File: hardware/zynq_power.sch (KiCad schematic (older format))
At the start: 61 parts, among them U1 xc7z030sbg485

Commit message: Added Power/Protection Circuit
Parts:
- renumbered C1 to C201, C2 to C202, C3 to C203, C4 to C204, C5 to C205, C6 to C206, C7 to C207, C8 to C208, C9 to C209, C10 to C210, C11 to C211, C12 to C212, C13 to C213, C14 to C214, C15 to C215, C16 to C216, C17 to C217, C18 to C218, C19 to C219, C20 to C220, C21 to C221, C22 to C222, C23 to C223, C24 to C224, C25 to C225, C26 to C226, C27 to C227, C28 to C228, C29 to C229, C30 to C230, C31 to C231, C32 to C232, C33 to C233, C34 to C234, C35 to C235, C36 to C236, C37 to C237, C38 to C238, C39 to C239, C40 to C240, C41 to C241, C42 to C242, C43 to C243, C44 to C244, C45 to C245, C46 to C246, C47 to C247, C48 to C248, C49 to C249, C50 to C250, C51 to C251, C52 to C252, C53 to C253, C54 to C254, C55 to C255, C56 to C256, C57 to C257, C58 to C258, L1 to L201, L2 to L202, U1 to U201

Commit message: Length matched DDR3 Memory again.
Forgot to keep enough space between the traces and between the meander waves.

Also, I switched to Kicad 5.0 RC2.

Swaped a few ddr signals.
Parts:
- C201, C203, C204, C205, C206, C208, C209, C210, C211, C212, C213, C214, C215, C216, C217, C218, C219, C220, C223, C224, C225, C226, C227, C228, C229, C230, C231, C233, C234, C235, C236, C237, C238, C239, C240, C241, C242, C243, C244, C245, C246, C247, C249, C250, C251, C252, C253, C255, C256, C257, C258: symbol C_Small -> device:C_Small
- C202: footprint C_2917 -> (none); symbol CP_Small -> device:CP_Small
- C207, C221, C222, C232, C248, C254: symbol CP_Small -> device:CP_Small
- L201, L202: symbol L_Small -> device:L_Small
- U201: symbol xc7z030sbg485 -> xilinx_zynq_clg485:xc7z030sbg485
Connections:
- wire segments 184 -> 292

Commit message: Layouted most of the Power Circuit and Triggerbus Levelshifters.
Added Footprint for Tantal Caps. Modified Footprint for MDR20 Connector, SD-Card.

Fixed Symbol and Circuit for Power Supervisor/Delay IC.

Also fixed some smaller things in the schematics.
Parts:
- C201, C203, C234, C239: footprint Capacitors_SMD:C_1210 -> Capacitor_SMD:C_0603_1608Metric; Description CAP CER 47UF 6.3V X5R 1210 -> CAP CER 47UF 6.3V X5R 0603; Digikey 490-1887-1-ND -> 490-13247-1-ND; MFG Part Num GRM32ER60J476ME20L -> GRM188R60J476ME15D; Populate for CLG484(Z-7012s/Z-7015) (none) -> 1; Populate for SBGA485(Z-7030) (none) -> 1; Voltage (none) -> 6,3 V
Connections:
- net labels added: MGTAVCC, MGTAVTT
- wire segments 292 -> 294
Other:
- note added: "Todo: for MGTAVCC and MGTAVTT each add two 100 nF 0201 Cap and 1x 4.7 µF"
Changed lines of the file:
@@
 F 0 "C234" H 5260 1570 50  0000 L CNN
 F 1 "47µF" H 5260 1420 50  0000 L CNN
-F 2 "Capacitors_SMD:C_1210" H 5250 1500 50  0001 C CNN
-F 3 "http://search.murata.co.jp/Ceramy/image/img/A01X/G101/ENG/GRM32ER60J476ME20-01.pdf" H 5250 1500 50  0001 C CNN
+F 2 "Capacitor_SMD:C_0603_1608Metric" H 5250 1500 50  0001 C CNN
+F 3 "http://search.murata.co.jp/Ceramy/image/img/A01X/G101/ENG/GRM188R60J476ME15-01.pdf" H 5250 1500 50  0001 C CNN
 F 4 "Murata" H 5250 1500 60  0001 C CNN "MFG Name"
-F 5 "GRM32ER60J476ME20L" H 5250 1500 60  0001 C CNN "MFG Part Num"
-F 6 "490-1887-1-ND" H 5250 1500 60  0001 C CNN "Digikey"
+F 5 "GRM188R60J476ME15D " H 5250 1500 60  0001 C CNN "MFG Part Num"
+F 6 "490-13247-1-ND" H 5250 1500 60  0001 C CNN "Digikey"
 F 7 "1" H 5250 1500 60  0001 C CNN "Populated"
-F 8 "CAP CER 47UF 6.3V X5R 1210" H 5250 1500 60  0001 C CNN "Description"
+F 8 "CAP CER 47UF 6.3V X5R 0603" H 5250 1500 60  0001 C CNN "Description"
 F 9 "SPEC" H 5250 1500 60  0001 C CNN "Source"
+F 10 "1" H 5250 1500 50  0001 C CNN "Populate for SBGA485(Z-7030)"
+F 11 "1" H 5250 1500 50  0001 C CNN "Populate for CLG484(Z-7012s/Z-7015)"
+F 12 "6,3 V" H 5350 1300 50  0000 C BNN "Voltage"
 	1    5250 1500
 	1    0    0    -1
@@
 $EndComp
 $Comp
-L device:C_Small C203
-U 1 1 5AE7068A
-P 1200 3550
-F 0 "C203" H 1210 3620 50  0000 L CNN
-F 1 "47µF" H 1210 3470 50  0000 L CNN
-F 2 "Capacitors_SMD:C_1210" H 1200 3550 50  0001 C CNN
-F 3 "http://search.murata.co.jp/Ceramy/image/img/A01X/G101/ENG/GRM32ER60J476ME20-01.pdf" H 1200 3550 50  0001 C CNN
-F 4 "Murata" H 1200 3550 60  0001 C CNN "MFG Name"
-F 5 "GRM32ER60J476ME20L" H 1200 3550 60  0001 C CNN "MFG Part Num"
-F 6 "490-1887-1-ND" H 1200 3550 60  0001 C CNN "Digikey"
-F 7 "1" H 1200 3550 60  0001 C CNN "Populated"
-F 8 "CAP CER 47UF 6.3V X5R 1210" H 1200 3550 60  0001 C CNN "Description"
-F 9 "SPEC" H 1200 3550 60  0001 C CNN "Source"
-	1    1200 3550
-	1    0    0    -1
-$EndComp
-$Comp
 L device:CP_Small C207
 U 1 1 5AE72084
@@
 VCCO_MIO1
 $Comp
-L device:C_Small C201
-U 1 1 5AE73C22
-P 800 5450
-F 0 "C201" H 810 5520 50  0000 L CNN
-F 1 "47µF" H 810 5370 50  0000 L CNN
-F 2 "Capacitors_SMD:C_1210" H 800 5450 50  0001 C CNN
-F 3 "http://search.murata.co.jp/Ceramy/image/img/A01X/G101/ENG/GRM32ER60J476ME20-01.pdf" H 800 5450 50  0001 C CNN
-F 4 "Murata" H 800 5450 60  0001 C CNN "MFG Name"
-F 5 "GRM32ER60J476ME20L" H 800 5450 60  0001 C CNN "MFG Part Num"
-F 6 "490-1887-1-ND" H 800 5450 60  0001 C CNN "Digikey"
-F 7 "1" H 800 5450 60  0001 C CNN "Populated"
-F 8 "CAP CER 47UF 6.3V X5R 1210" H 800 5450 60  0001 C CNN "Description"
-F 9 "SPEC" H 800 5450 60  0001 C CNN "Source"
-	1    800  5450
-	1    0    0    -1
-$EndComp
-$Comp
 L power1:GND #PWR06
 U 1 1 5AE7C463
@@
 Text GLabel 4450 5100 1    60   Output ~ 0
 VCCO_34
-$Comp
-L device:C_Small C239
-U 1 1 5AE90BAB
-P 5950 5450
-F 0 "C239" H 5960 5520 50  0000 L CNN
-F 1 "47µF" H 5960 5370 50  0000 L CNN
-F 2 "Capacitors_SMD:C_1210" H 5950 5450 50  0001 C CNN
-F 3 "http://search.murata.co.jp/Ceramy/image/img/A01X/G101/ENG/GRM32ER60J476ME20-01.pdf" H 5950 5450 50  0001 C CNN
-F 4 "Murata" H 5950 5450 60  0001 C CNN "MFG Name"
-F 5 "GRM32ER60J476ME20L" H 5950 5450 60  0001 C CNN "MFG Part Num"
-F 6 "490-1887-1-ND" H 5950 5450 60  0001 C CNN "Digikey"
-F 7 "1" H 5950 5450 60  0001 C CNN "Populated"
-F 8 "CAP CER 47UF 6.3V X5R 1210" H 5950 5450 60  0001 C CNN "Description"
-F 9 "SPEC" H 5950 5450 60  0001 C CNN "Source"
-	1    5950 5450
-	1    0    0    -1
-$EndComp
 $Comp
 L power1:GND #PWR017
@@
 Wire Wire Line
 	1200 3300 1200 3200
+$Comp
+L device:C_Small C203
+U 1 1 5B120C73
+P 1200 3550
+F 0 "C203" H 1210 3620 50  0000 L CNN
+F 1 "47µF" H 1210 3470 50  0000 L CNN
+F 2 "Capacitor_SMD:C_0603_1608Metric" H 1200 3550 50  0001 C CNN
+F 3 "http://search.murata.co.jp/Ceramy/image/img/A01X/G101/ENG/GRM188R60J476ME15-01.pdf" H 1200 3550 50  0001 C CNN
+F 4 "Murata" H 1200 3550 60  0001 C CNN "MFG Name"
+F 5 "GRM188R60J476ME15D " H 1200 3550 60  0001 C CNN "MFG Part Num"
+F 6 "490-13247-1-ND" H 1200 3550 60  0001 C CNN "Digikey"
+F 7 "1" H 1200 3550 60  0001 C CNN "Populated"
+F 8 "CAP CER 47UF 6.3V X5R 0603" H 1200 3550 60  0001 C CNN "Description"
+F 9 "SPEC" H 1200 3550 60  0001 C CNN "Source"
+F 10 "1" H 1200 3550 50  0001 C CNN "Populate for SBGA485(Z-7030)"
+F 11 "1" H 1200 3550 50  0001 C CNN "Populate for CLG484(Z-7012s/Z-7015)"
+F 12 "6,3 V" H 1300 3350 50  0000 C BNN "Voltage"
+	1    1200 3550
+	1    0    0    -1
+$EndComp
+$Comp
+L device:C_Small C239
+U 1 1 5B120EBB
+P 5950 5450
+F 0 "C239" H 5960 5520 50  0000 L CNN
+F 1 "47µF" H 5960 5370 50  0000 L CNN
+F 2 "Capacitor_SMD:C_0603_1608Metric" H 5950 5450 50  0001 C CNN
+F 3 "http://search.murata.co.jp/Ceramy/image/img/A01X/G101/ENG/GRM188R60J476ME15-01.pdf" H 5950 5450 50  0001 C CNN
+F 4 "Murata" H 5950 5450 60  0001 C CNN "MFG Name"
+F 5 "GRM188R60J476ME15D " H 5950 5450 60  0001 C CNN "MFG Part Num"
+F 6 "490-13247-1-ND" H 5950 5450 60  0001 C CNN "Digikey"
+F 7 "1" H 5950 5450 60  0001 C CNN "Populated"
+F 8 "CAP CER 47UF 6.3V X5R 0603" H 5950 5450 60  0001 C CNN "Description"
+F 9 "SPEC" H 5950 5450 60  0001 C CNN "Source"
+F 10 "1" H 5950 5450 50  0001 C CNN "Populate for SBGA485(Z-7030)"
+F 11 "1" H 5950 5450 50  0001 C CNN "Populate for CLG484(Z-7012s/Z-7015)"
+F 12 "6,3 V" H 6050 5250 50  0000 C BNN "Voltage"
+	1    5950 5450
+	1    0    0    -1
+$EndComp
+$Comp
+L device:C_Small C201
+U 1 1 5B121187
+P 800 5450
+F 0 "C201" H 810 5520 50  0000 L CNN
+F 1 "47µF" H 810 5370 50  0000 L CNN
+F 2 "Capacitor_SMD:C_0603_1608Metric" H 800 5450 50  0001 C CNN
+F 3 "http://search.murata.co.jp/Ceramy/image/img/A01X/G101/ENG/GRM188R60J476ME15-01.pdf" H 800 5450 50  0001 C CNN
+F 4 "Murata" H 800 5450 60  0001 C CNN "MFG Name"
+F 5 "GRM188R60J476ME15D " H 800 5450 60  0001 C CNN "MFG Part Num"
+F 6 "490-13247-1-ND" H 800 5450 60  0001 C CNN "Digikey"
+F 7 "1" H 800 5450 60  0001 C CNN "Populated"
+F 8 "CAP CER 47UF 6.3V X5R 0603" H 800 5450 60  0001 C CNN "Description"
+F 9 "SPEC" H 800 5450 60  0001 C CNN "Source"
+F 10 "1" H 800 5450 50  0001 C CNN "Populate for SBGA485(Z-7030)"
+F 11 "1" H 800 5450 50  0001 C CNN "Populate for CLG484(Z-7012s/Z-7015)"
+F 12 "6,3 V" H 900 5250 50  0000 C BNN "Voltage"
+	1    800  5450
+	1    0    0    -1
+$EndComp
+Wire Wire Line
+	9800 1350 7200 1350
+Connection ~ 9800 1350
+Wire Wire Line
+	9250 1450 7200 1450
+Connection ~ 9250 1450
+Text Label 7200 1350 0    50   ~ 0
+MGTAVCC
+Text Label 7200 1450 0    50   ~ 0
+MGTAVTT
+Text Label 1600 6550 0    50   ~ 0
+MGTAVCC
+Text Label 2750 6500 0    50   ~ 0
+MGTAVTT
+Text Notes 1200 6800 0    50   ~ 0
+Todo: for MGTAVCC and MGTAVTT each add two 100 nF 0201 Cap and 1x 4.7 µF
 $EndSCHEMATC

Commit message: Improved Powerdistribution Network of the FPGA.
Also started to layout USB.
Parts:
- added C259, C262: 4.7µF, Capacitor_SMD:C_0603_1608Metric, symbol device:C_Small
- added C260, C261, C263, C264: 100 nF, Capacitor_SMD:C_0201_0603Metric, symbol device:C_Small
- C204, C206, C236, C237: footprint Capacitors_SMD:C_0805 -> Capacitor_SMD:C_0603_1608Metric; Description CAP CER 4.7UF 10V X7R 0805 -> CAP CER 4.7UF 6.3V X7R 0603; Digikey 490-6479-1-ND -> 587-4906-1-ND; MFG Name Murata -> Taiyo Yuden; MFG Part Num GRM21BR71A475KA73 -> JMK107BB7475MA-T; Populate for CLG484(Z-7012s/Z-7015) Populate -> 1; Populate for SBGA485(Z-7030) DNP -> 1; Voltage (none) -> 6,3 V
- C205, C224, C251, C256: footprint Capacitors_SMD:C_0805 -> Capacitor_SMD:C_0603_1608Metric; Description CAP CER 4.7UF 10V X7R 0805 -> CAP CER 4.7UF 6.3V X7R 0603; Digikey 490-6479-1-ND -> 587-4906-1-ND; MFG Name Murata -> Taiyo Yuden; MFG Part Num GRM21BR71A475KA73 -> JMK107BB7475MA-T; Populate for CLG484(Z-7012s/Z-7015) (none) -> Populate; Populate for SBGA485(Z-7030) (none) -> DNP; Voltage (none) -> 6,3 V
- C207, C221, C222, C232, C248, C254: footprint Capacitors_SMD:C_1210 -> Capacitor_SMD:C_1210_3225Metric
- C208, C211, C223, C225, C243, C245: footprint Capacitors_SMD:C_0805 -> Capacitor_SMD:C_0603_1608Metric; Description CAP CER 4.7UF 10V X7R 0805 -> CAP CER 4.7UF 6.3V X7R 0603; Digikey 490-6479-1-ND -> 587-4906-1-ND; MFG Name Murata -> Taiyo Yuden; MFG Part Num GRM21BR71A475KA73 -> JMK107BB7475MA-T; Voltage (none) -> 6,3 V
- C209, C210, C212, C213, C214, C215, C216, C217, C218, C219, C220, C228, C230, C231, C233, C235, C238, C240, C241, C242, C244, C246, C247, C249, C250, C252: footprint Capacitors_SMD:C_0603 -> Capacitor_SMD:C_0402_1005Metric; Description CAP CER 0.47UF 6.3V X7R 0603,1 mΩ < ESR < 20 mΩ, ESL 0.5 nH -> CAP CER 0.47UF 6.3V X7R 0402; Digikey 490-6416-1-ND -> 587-3765-1-ND; MFG Name Murata -> Taiyo Yuden; MFG Part Num GRM188R70J474KA01 -> JMK105B7474KVHF; Voltage (none) -> 6.3 V
- C226: footprint Capacitors_SMD:C_0805 -> Capacitor_SMD:C_0603_1608Metric; Description CAP CER 4.7UF 10V X7R 0805 -> CAP CER 4.7UF 6.3V X7R 0603; Digikey 490-6479-1-ND -> 587-4906-1-ND; MFG Name Murata -> Taiyo Yuden; MFG Part Num GRM21BR71A475KA73 -> JMK107BB7475MA-T; Populate for CLG484(Z-7012s/Z-7015) (none) -> 1; Populate for SBGA485(Z-7030) (none) -> 1; Voltage (none) -> 6,3 V
- C227, C229, C253, C257: footprint Capacitors_SMD:C_0603 -> Capacitor_SMD:C_0402_1005Metric; Description CAP CER 0.47UF 6.3V X7R 0603,1 mΩ < ESR < 20 mΩ, ESL 0.5 nH -> CAP CER 0.47UF 6.3V X7R 0402; Digikey 490-6416-1-ND -> 587-3765-1-ND; MFG Name Murata -> Taiyo Yuden; MFG Part Num GRM188R70J474KA01 -> JMK105B7474KVHF; Populate for CLG484(Z-7012s/Z-7015) (none) -> 1; Populate for SBGA485(Z-7030) (none) -> 1; Voltage (none) -> 6.3 V
- C255: footprint Capacitors_SMD:C_0603 -> Capacitor_SMD:C_0603_1608Metric
- C258: footprint Capacitors_SMD:C_0603 -> Capacitor_SMD:C_0402_1005Metric; Description CAP CER 0.47UF 6.3V X5R 0603 -> CAP CER 0.47UF 6.3V X7R 0402; Digikey 490-3266-1-ND -> 587-3765-1-ND; MFG Name Murata -> Taiyo Yuden; MFG Part Num GRM155R60J474KE19D -> JMK105B7474KVHF; Populate for CLG484(Z-7012s/Z-7015) (none) -> 1; Populate for SBGA485(Z-7030) (none) -> 1; Voltage (none) -> 6.3 V
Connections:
- wire segments 294 -> 318

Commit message: Fixed Schematic Symbols
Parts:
- C201, C203, C204, C205, C206, C208, C209, C210, C211, C212, C213, C214, C215, C216, C217, C218, C219, C220, C223, C224, C225, C226, C227, C228, C229, C230, C231, C233, C234, C235, C236, C237, C238, C239, C240, C241, C242, C243, C244, C245, C246, C247, C249, C250, C251, C252, C253, C255, C256, C257, C258, C259, C260, C261, C262, C263, C264: symbol device:C_Small -> Device:C_Small
- C202, C207, C221, C222, C232, C248, C254: symbol device:CP_Small -> Device:CP_Small
- L201, L202: symbol device:L_Small -> Device:L_Small

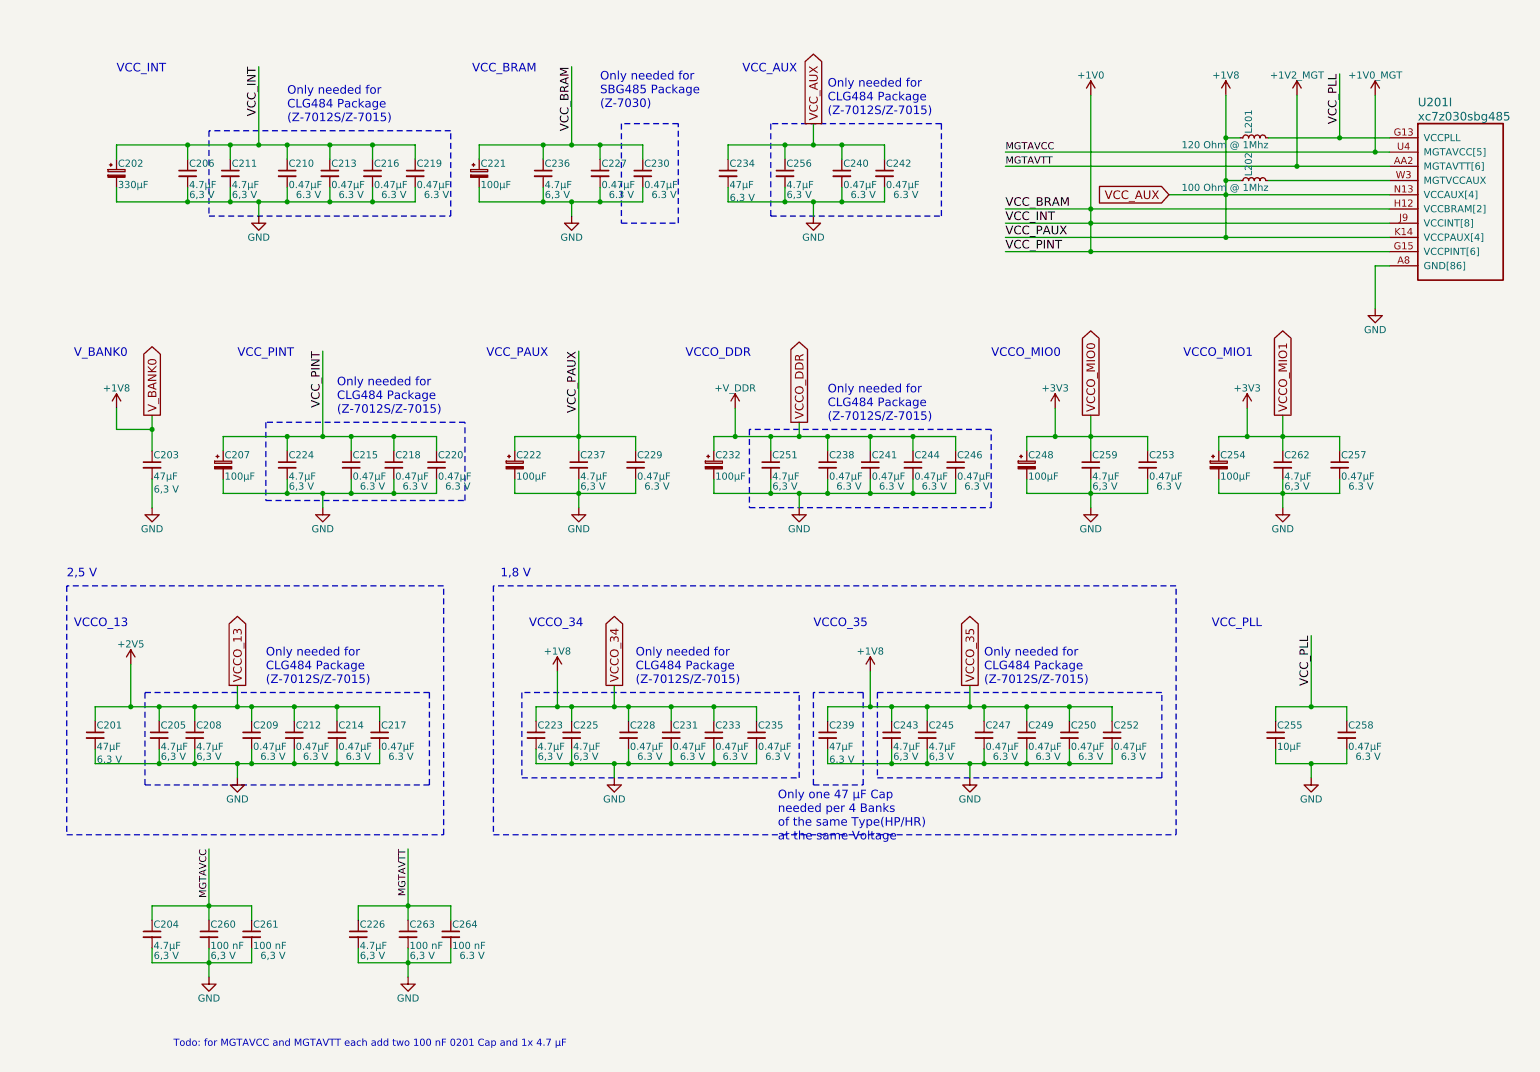
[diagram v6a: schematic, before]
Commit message: SFP+ Power Filter, Levelshifter and MGT/TLK Clock Distribution.
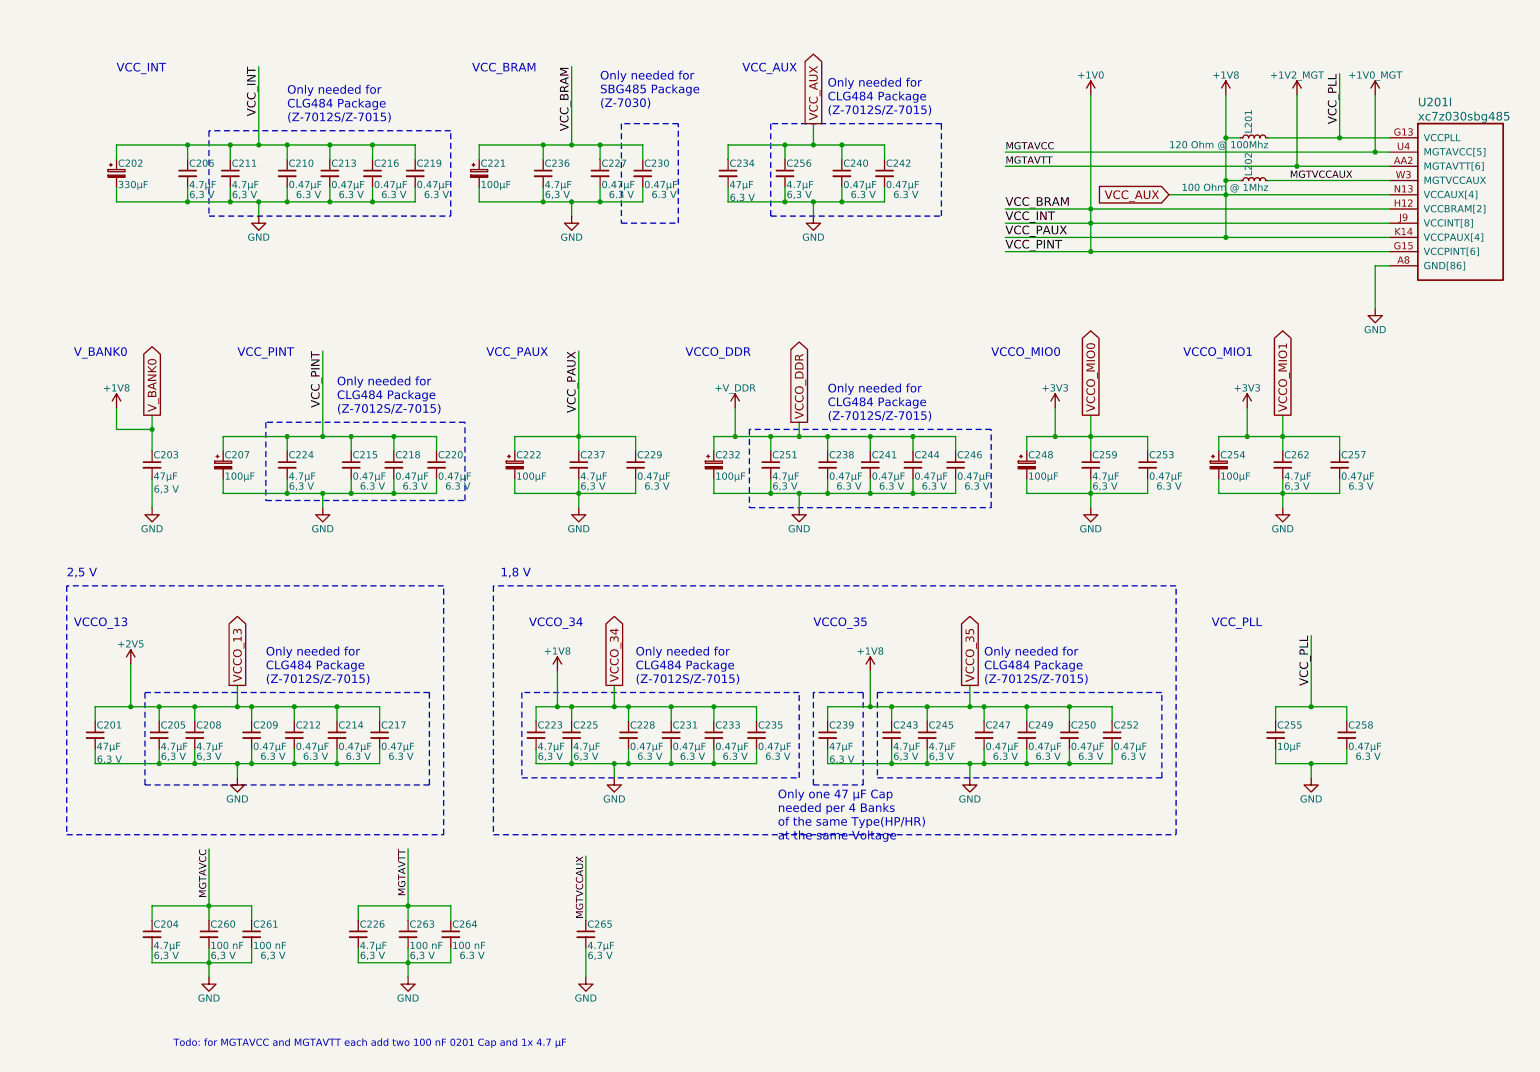
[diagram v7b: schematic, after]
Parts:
- added C265: 4.7µF, Capacitor_SMD:C_0603_1608Metric, symbol Device:C_Small
- L201: value 120 Ohm @ 1Mhz -> 120 Ohm @ 100Mhz
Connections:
- net GND: now also C265.2
- net MGTVCCAUX: now reaches L202.2, U201.W3 (MGTVCCAUX)
- net MGTVCCAUX: now also C265.1
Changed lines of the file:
@@
 P 8950 1250
 F 0 "L201" H 8980 1290 50  0000 L CNN
-F 1 "120 Ohm @ 1Mhz" V 8900 1150 50  0000 L CNN
+F 1 "120 Ohm @ 100Mhz" V 8900 1150 50  0000 L CNN
 F 2 "Inductors_SMD:L_0603" H 8950 1250 50  0001 C CNN
 F 3 "https://www.murata.com/en-us/products/productdata/8796738650142/ENFA0003.pdf" H 8950 1250 50  0001 C CNN
@@
 Wire Wire Line
 	1750 1300 1750 1400
+Text Label 9200 1550 0    50   ~ 0
+MGTVCCAUX
+Text Label 4250 6300 3    50   ~ 0
+MGTVCCAUX
+$Comp
+L Device:C_Small C265
+U 1 1 5BB74A7C
+P 4250 6850
+F 0 "C265" H 4260 6920 50  0000 L CNN
+F 1 "4.7µF" H 4260 6770 50  0000 L CNN
+F 2 "Capacitor_SMD:C_0603_1608Metric" H 4250 6850 50  0001 C CNN
+F 3 "http://ds.yuden.co.jp/TYCOMPAS/ut/detail.do?productNo=JMK107BB7475MA-T&fileName=JMK107BB7475MA-T_SS&mode=specSheetDownload" H 4250 6850 50  0001 C CNN
+F 4 "Taiyo Yuden" H 4250 6850 60  0001 C CNN "MFG Name"
+F 5 "JMK107BB7475MA-T" H 4250 6850 60  0001 C CNN "MFG Part Num"
+F 6 "587-4906-1-ND" H 4250 6850 60  0001 C CNN "Digikey"
+F 7 "1" H 4250 6850 60  0001 C CNN "Populated"
+F 8 "CAP CER 4.7UF 6.3V X7R 0603" H 4250 6850 60  0001 C CNN "Description"
+F 9 "SPEC" H 4250 6850 60  0001 C CNN "Source"
+F 10 "1" H 4250 6850 60  0001 C CNN "Populate for SBGA485(Z-7030)"
+F 11 "1" H 4250 6850 60  0001 C CNN "Populate for CLG484(Z-7012s/Z-7015)"
+F 12 "6,3 V" H 4350 6700 50  0000 C CNN "Voltage"
+	1    4250 6850
+	1    0    0    -1
+$EndComp
+$Comp
+L power:GND #PWR0241
+U 1 1 5BB74B59
+P 4250 7150
+F 0 "#PWR0241" H 4250 6900 50  0001 C CNN
+F 1 "GND" H 4250 7000 50  0000 C CNN
+F 2 "" H 4250 7150 50  0001 C CNN
+F 3 "" H 4250 7150 50  0001 C CNN
+	1    4250 7150
+	1    0    0    -1
+$EndComp
+Wire Wire Line
+	4250 6950 4250 7150
+Wire Wire Line
+	4250 6300 4250 6750
 $EndSCHEMATC
